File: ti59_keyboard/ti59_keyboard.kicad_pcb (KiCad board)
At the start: 2 copper layers, 68 x 95.7 mm, 59 parts, among them J1 C1, J10 C4, J11 R5, J12 R6, J13 C5, J14 R0, J2 R7, J3 R2, J4 C2, J5 R8, J6 R1, J7 C3, J8 R4, J9 R3, SW1 KEY, SW10 KEY, SW11 KEY, SW12 KEY, SW13 KEY, SW14 KEY, SW15 KEY, SW16 KEY, SW17 KEY, SW18 KEY, SW19 KEY, SW2 KEY, SW20 KEY, SW21 KEY, SW22 KEY, SW23 KEY, SW24 KEY, SW25 KEY, SW26 KEY, SW27 KEY, SW28 KEY, SW29 KEY, SW3 KEY, SW30 KEY, SW31 KEY, SW32 KEY, SW33 KEY, SW34 KEY, SW35 KEY, SW36 KEY, SW37 KEY, SW38 KEY, SW39 KEY, SW4 KEY, SW40 KEY, SW41 KEY, SW42 KEY, SW43 KEY, SW44 KEY, SW45 KEY, SW5 KEY, SW6 KEY, SW7 KEY, SW8 KEY, SW9 KEY

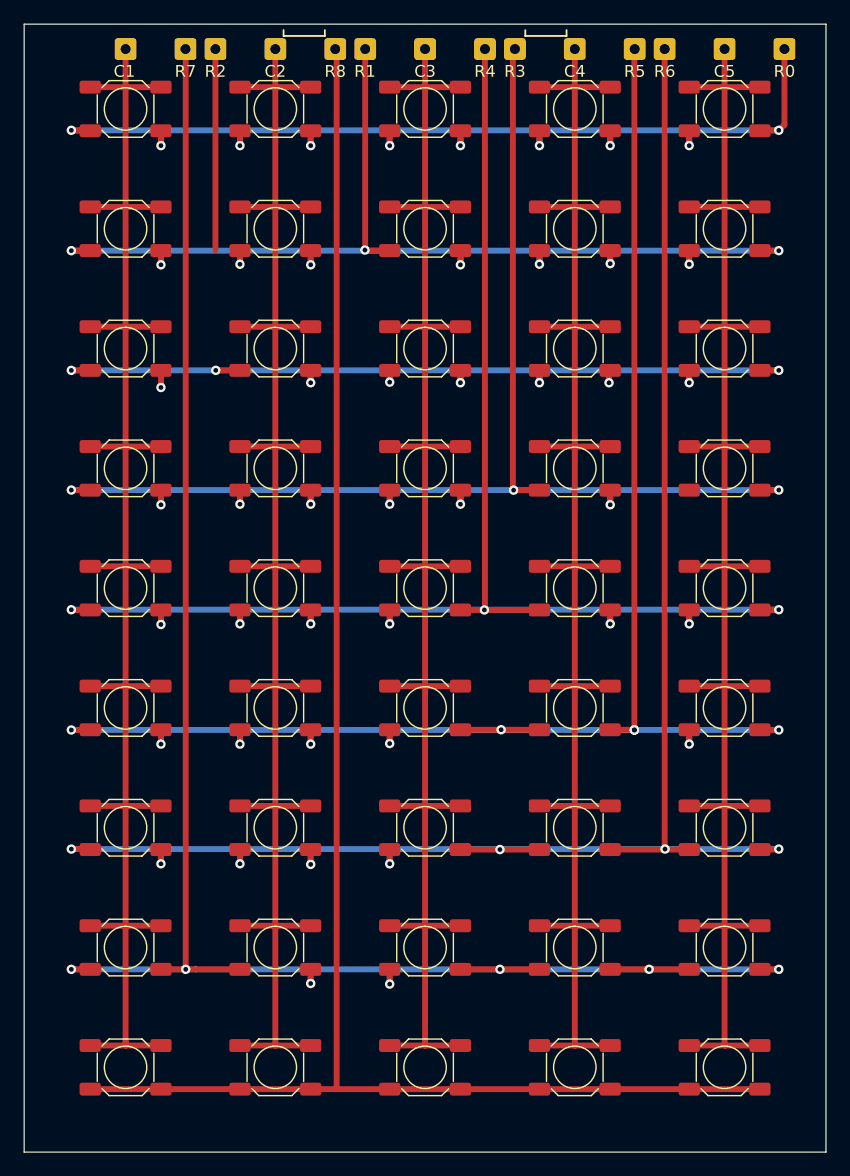
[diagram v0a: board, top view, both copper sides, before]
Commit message: Correct error with R2 missing track
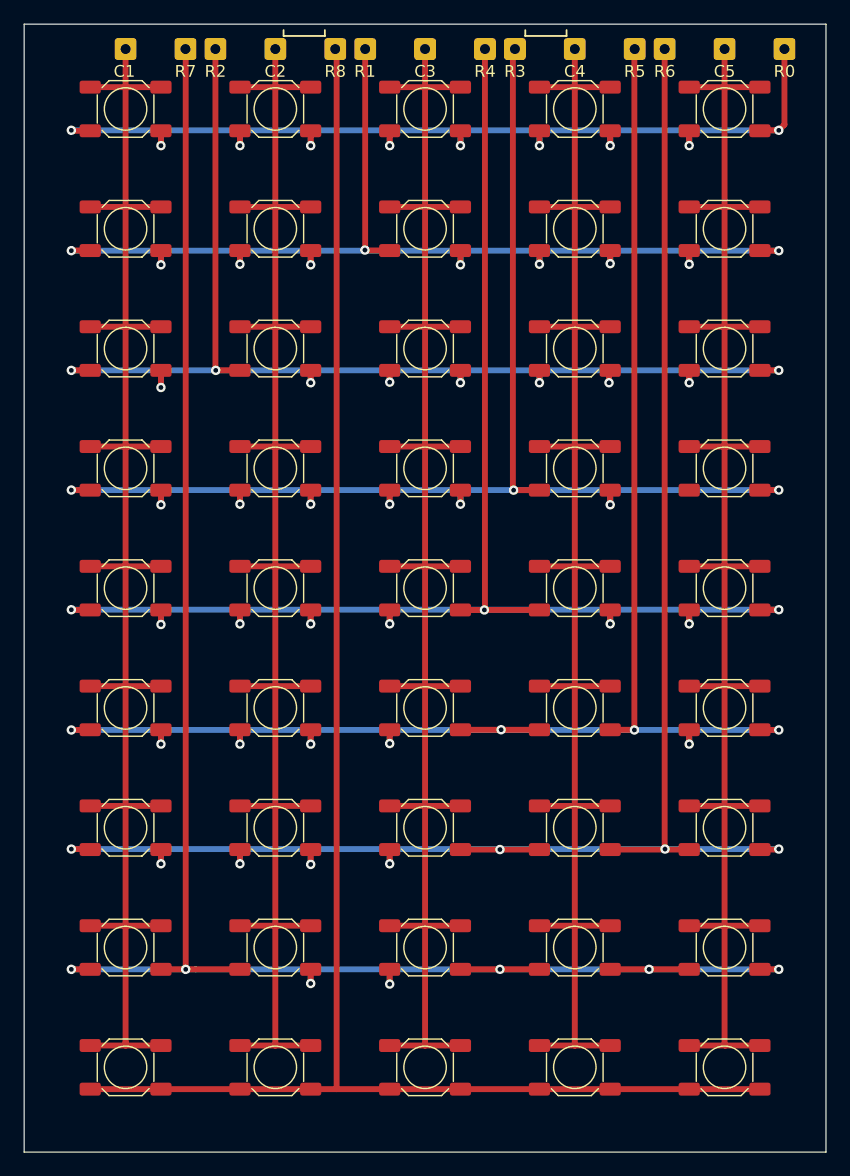
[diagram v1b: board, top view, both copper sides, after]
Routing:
- net /R2: track 97.9 -> 108.1 mm
- net /R5: vias 10 -> 9
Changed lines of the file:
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@@
+		(layer "Dwgs.User")
+		(pts
+			(xy -34 0) (xy -34 95.66)
+		)
+		(height 16.499999)
+		(gr_text "95.6600 mm"
+			(at -51.649999 47.83 90)
+			(layer "Dwgs.User")
+			(effects
+				(font
+					(size 1 1)
+					(thickness 0.15)
+				)
+			)
+		)
+		(format
+			(prefix "")
+			(suffix "")
+			(units 3)
+			(units_format 1)
+			(precision 4)
+		)
+		(style
+			(thickness 0.15)
+			(arrow_length 1.27)
+			(text_position_mode 0)
+			(extension_height 0.58642)
+			(extension_offset 0.5) keep_text_aligned)
+	)
+	(dimension
+		(type aligned)
 		(layer "Dwgs.User")
 		(pts
@@
 		(layer "Dwgs.User")
 		(pts
+			(xy -34 0) (xy 34 0)
+		)
+		(height -7)
+		(gr_text "68.0000 mm"
+			(at 0 -8.15 0)
+			(layer "Dwgs.User")
+			(effects
+				(font
+					(size 1 1)
+					(thickness 0.15)
+				)
+			)
+		)
+		(format
+			(prefix "")
+			(suffix "")
+			(units 3)
+			(units_format 1)
+			(precision 4)
+		)
+		(style
+			(thickness 0.15)
+			(arrow_length 1.27)
+			(text_position_mode 0)
+			(extension_height 0.58642)
+			(extension_offset 0.5) keep_text_aligned)
+	)
+	(dimension
+		(type aligned)
+		(layer "Dwgs.User")
+		(pts
 			(xy -25.4 37.67) (xy -25.4 47.83)
 		)
@@
 	(segment
 		(start -17.78 2.11)
-		(end -17.78 19.17)
+		(end -17.78 29.33)
 		(width 0.5)
 		(layer "F.Cu")
@@
 	)
 	(segment
+		(start -17.78 29.33)
+		(end -17.75 29.36)
+		(width 0.5)
+		(layer "F.Cu")
+		(net 3)
+	)
+	(segment
 		(start -15.7 29.36)
 		(end -17.75 29.36)
@@
 	)
 	(segment
+		(start 15.6 30.41)
+		(end 15.6 29.46)
+		(width 0.5)
+		(layer "F.Cu")
+		(net 3)
+	)
+	(segment
+		(start -28.4 29.36)
+		(end -30 29.36)
+		(width 0.5)
+		(layer "F.Cu")
+		(net 3)
+	)
+	(via
+		(at -3 30.36)
+		(size 0.8)
+		(drill 0.4)
+		(layers "F.Cu" "B.Cu")
+		(net 3)
+	)
+	(via
+		(at 15.6 30.41)
+		(size 0.8)
+		(drill 0.4)
+		(layers "F.Cu" "B.Cu")
+		(net 3)
+	)
+	(via
+		(at -30 29.36)
+		(size 0.8)
+		(drill 0.4)
+		(layers "F.Cu" "B.Cu")
+		(net 3)
+	)
+	(via
+		(at 3 30.41)
+		(size 0.8)
+		(drill 0.4)
+		(layers "F.Cu" "B.Cu")
+		(net 3)
+	)
+	(via
+		(at 22.4 30.41)
+		(size 0.8)
+		(drill 0.4)
+		(layers "F.Cu" "B.Cu")
+		(net 3)
+	)
+	(via
+		(at -9.7 30.41)
+		(size 0.8)
+		(drill 0.4)
+		(layers "F.Cu" "B.Cu")
+		(net 3)
+	)
+	(via
+		(at 30 29.36)
+		(size 0.8)
+		(drill 0.4)
+		(layers "F.Cu" "B.Cu")
+		(net 3)
+	)
+	(via
+		(at 9.7 30.41)
+		(size 0.8)
+		(drill 0.4)
+		(layers "F.Cu" "B.Cu")
+		(net 3)
+	)
+	(via
+		(at -22.4 30.81)
+		(size 0.8)
+		(drill 0.4)
+		(layers "F.Cu" "B.Cu")
+		(net 3)
+	)
+	(via
+		(at -17.75 29.36)
+		(size 0.8)
+		(drill 0.4)
+		(layers "F.Cu" "B.Cu")
+		(net 3)
+	)
+	(segment
+		(start -22.4 29.41)
+		(end -22.35 29.36)
+		(width 0.5)
+		(layer "B.Cu")
+		(net 3)
+	)
+	(segment
+		(start -9.65 29.36)
+		(end -2.9 29.36)
+		(width 0.5)
+		(layer "B.Cu")
+		(net 3)
+	)
+	(segment
+		(start -22.35 29.36)
+		(end -17.75 29.36)
+		(width 0.5)
+		(layer "B.Cu")
+		(net 3)
+	)
+	(segment
+		(start -9.7 30.41)
+		(end -9.7 29.41)
+		(width 0.5)
+		(layer "B.Cu")
+		(net 3)
+	)
+	(segment
+		(start -17.75 29.36)
+		(end -9.65 29.36)
+		(width 0.5)
+		(layer "B.Cu")
+		(net 3)
+	)
+	(segment
+		(start 3 30.41)
+		(end 3 29.41)
+		(width 0.5)
+		(layer "B.Cu")
+		(net 3)
+	)
+	(segment
+		(start -3 29.46)
+		(end -2.9 29.36)
+		(width 0.5)
+		(layer "B.Cu")
+		(net 3)
+	)
+	(segment
+		(start 9.7 30.41)
+		(end 9.7 29.36)
+		(width 0.5)
+		(layer "B.Cu")
+		(net 3)
+	)
+	(segment
+		(start -2.9 29.36)
+		(end 3.05 29.36)
+		(width 0.5)
+		(layer "B.Cu")
+		(net 3)
+	)
+	(segment
+		(start 22.4 30.41)
+		(end 22.4 29.36)
+		(width 0.5)
+		(layer "B.Cu")
+		(net 3)
+	)
+	(segment
+		(start -22.4 30.81)
+		(end -22.4 29.41)
+		(width 0.5)
+		(layer "B.Cu")
+		(net 3)
+	)
+	(segment
+		(start -3 30.36)
+		(end -3 29.46)
+		(width 0.5)
+		(layer "B.Cu")
+		(net 3)
+	)
+	(segment
 		(start -17.78 29.33)
 		(end -17.75 29.36)
 		(width 0.5)
-		(layer "F.Cu")
-		(net 3)
-	)
-	(segment
-		(start 15.6 30.41)
-		(end 15.6 29.46)
-		(width 0.5)
-		(layer "F.Cu")
-		(net 3)
-	)
-	(segment
-		(start -28.4 29.36)
-		(end -30 29.36)
-		(width 0.5)
-		(layer "F.Cu")
-		(net 3)
-	)
-	(via
-		(at -3 30.36)
-		(size 0.8)
-		(drill 0.4)
-		(layers "F.Cu" "B.Cu")
-		(net 3)
-	)
-	(via
-		(at 15.6 30.41)
-		(size 0.8)
-		(drill 0.4)
-		(layers "F.Cu" "B.Cu")
-		(net 3)
-	)
-	(via
-		(at -30 29.36)
-		(size 0.8)
-		(drill 0.4)
-		(layers "F.Cu" "B.Cu")
-		(net 3)
-	)
-	(via
-		(at 3 30.41)
-		(size 0.8)
-		(drill 0.4)
-		(layers "F.Cu" "B.Cu")
-		(net 3)
-	)
-	(via
-		(at 22.4 30.41)
-		(size 0.8)
-		(drill 0.4)
-		(layers "F.Cu" "B.Cu")
-		(net 3)
-	)
-	(via
-		(at -9.7 30.41)
-		(size 0.8)
-		(drill 0.4)
-		(layers "F.Cu" "B.Cu")
-		(net 3)
-	)
-	(via
-		(at 30 29.36)
-		(size 0.8)
-		(drill 0.4)
-		(layers "F.Cu" "B.Cu")
-		(net 3)
-	)
-	(via
-		(at 9.7 30.41)
-		(size 0.8)
-		(drill 0.4)
-		(layers "F.Cu" "B.Cu")
-		(net 3)
-	)
-	(via
-		(at -22.4 30.81)
-		(size 0.8)
-		(drill 0.4)
-		(layers "F.Cu" "B.Cu")
-		(net 3)
-	)
-	(via
-		(at -17.75 29.36)
-		(size 0.8)
-		(drill 0.4)
-		(layers "F.Cu" "B.Cu")
-		(net 3)
-	)
-	(segment
-		(start -22.4 29.41)
-		(end -22.35 29.36)
-		(width 0.5)
-		(layer "B.Cu")
-		(net 3)
-	)
-	(segment
-		(start -9.65 29.36)
-		(end -2.9 29.36)
-		(width 0.5)
-		(layer "B.Cu")
-		(net 3)
-	)
-	(segment
-		(start -22.35 29.36)
-		(end -17.75 29.36)
-		(width 0.5)
-		(layer "B.Cu")
-		(net 3)
-	)
-	(segment
-		(start -9.7 30.41)
-		(end -9.7 29.41)
-		(width 0.5)
-		(layer "B.Cu")
-		(net 3)
-	)
-	(segment
-		(start -17.75 29.36)
-		(end -9.65 29.36)
-		(width 0.5)
-		(layer "B.Cu")
-		(net 3)
-	)
-	(segment
-		(start 3 30.41)
-		(end 3 29.41)
-		(width 0.5)
-		(layer "B.Cu")
-		(net 3)
-	)
-	(segment
-		(start -3 29.46)
-		(end -2.9 29.36)
-		(width 0.5)
-		(layer "B.Cu")
-		(net 3)
-	)
-	(segment
-		(start 9.7 30.41)
-		(end 9.7 29.36)
-		(width 0.5)
-		(layer "B.Cu")
-		(net 3)
-	)
-	(segment
-		(start -2.9 29.36)
-		(end 3.05 29.36)
-		(width 0.5)
-		(layer "B.Cu")
-		(net 3)
-	)
-	(segment
-		(start 22.4 30.41)
-		(end 22.4 29.36)
-		(width 0.5)
-		(layer "B.Cu")
-		(net 3)
-	)
-	(segment
-		(start -22.4 30.81)
-		(end -22.4 29.41)
-		(width 0.5)
-		(layer "B.Cu")
-		(net 3)
-	)
-	(segment
-		(start -3 30.36)
-		(end -3 29.46)
-		(width 0.5)
-		(layer "B.Cu")
-		(net 3)
-	)
-	(segment
-		(start -17.78 29.33)
-		(end -17.75 29.36)
-		(width 0.5)
 		(layer "B.Cu")
 		(net 3)
@@
 		(size 0.8)
 		(drill 0.4)
-		(layers "F.Cu" "B.Cu")
-		(net 11)
-	)
-	(via
-		(at 17.75 59.86)
-		(size 0.8)
-		(drill 0.4)
